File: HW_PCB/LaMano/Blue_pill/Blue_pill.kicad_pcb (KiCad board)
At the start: 2 copper layers, 41.1 x 42.8 mm, 28 parts, among them J1 V_Battery, J2 STLINK, J5 MPU6050, J6 NRF24, SW1 SW_DPST_x2, SW2 SW_DPST_x2, U1 STM32F103C8Tx, U2 AMS1117-3.3, X1 Crystal

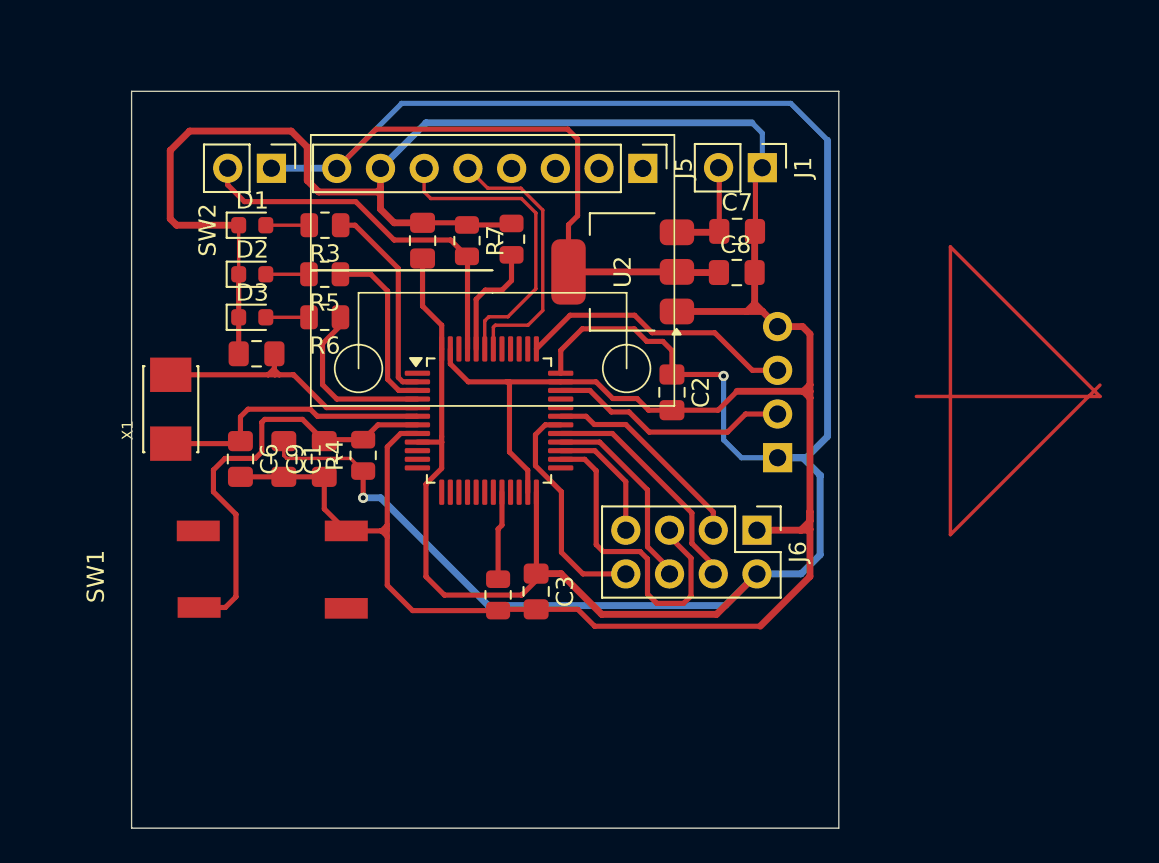
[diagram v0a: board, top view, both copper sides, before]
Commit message: DRC 0 Errors (Board cleareance errors, Fix: Increased Board size) Fixed mismatch size on 2 gnd tracks
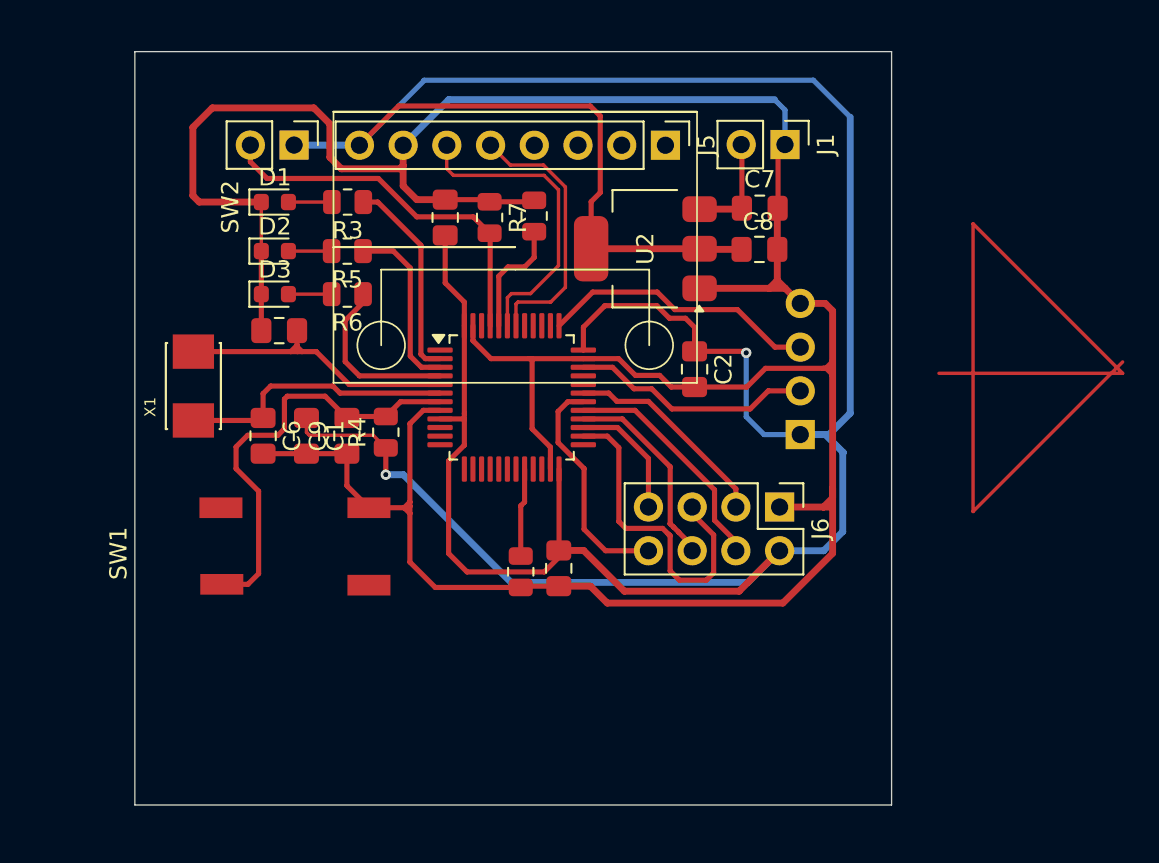
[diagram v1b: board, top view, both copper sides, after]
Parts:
- moved C1 1.88 mm to (48.8, 62.4)
- moved C3 1.88 mm to (63.4, 70.1)
- moved C5 1.88 mm to (47.2, 56.3)
- moved C6 1.88 mm to (46.3, 62.4)
- moved C7 1.88 mm to (75.1, 49.2)
- moved C8 1.88 mm to (75.1, 51.6)
- moved C9 1.88 mm to (51.1, 62.4)
- moved D1 1.88 mm to (47.0, 48.9)
- moved J1 1.88 mm to (76.6, 45.5)
- moved J2 1.88 mm to (77.5, 62.4)
- moved J5 1.88 mm to (69.6, 45.6)
- moved J6 1.88 mm to (76.3, 66.6)
- moved R1 1.88 mm to (61.2, 70.3)
- moved R2 1.88 mm to (62.0, 49.7)
- moved R3 1.88 mm to (51.2, 48.9)
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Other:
- board size 41.1 x 42.8 mm -> 44 x 43.8 mm

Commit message: 6-29 Added Potentiometer Added Voltage divider for Battery Sensor Changed Layer tracks of NRF24
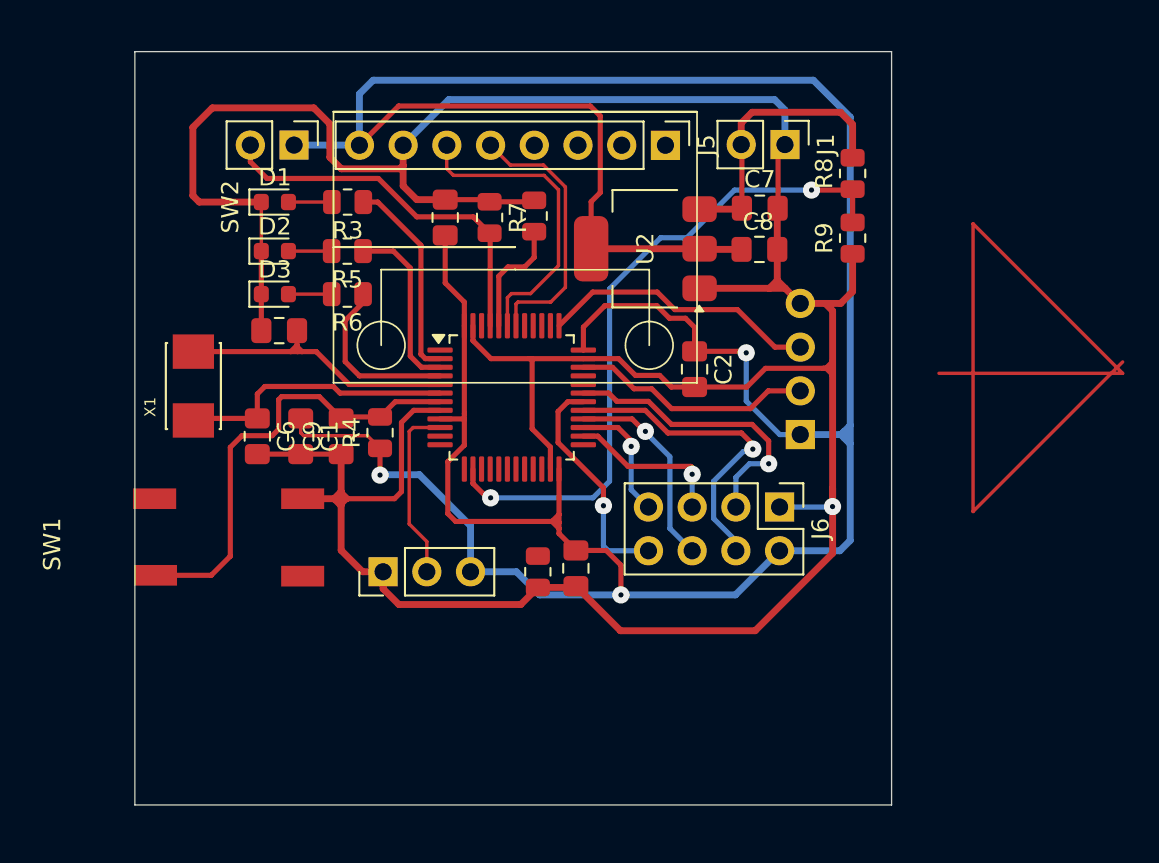
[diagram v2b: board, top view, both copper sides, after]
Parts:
- added J8: PINHD_1x3_Male, Connector_PinHeader_2.54mm:PinHeader_1x03_P2.54mm_Vertical, F.Cu at (53.2, 70.3)
- added R8: PORDEFINIR, Resistor_SMD:R_0805_2012Metric, F.Cu at (80.5, 47.2)
- added R9: PORDEFINIR, Resistor_SMD:R_0805_2012Metric, F.Cu at (80.5, 51.0)
- moved SW1 3.89 mm to (34.5, 68.7)
- moved C3 0.99 mm to (64.4, 70.1)
- moved R1 0.99 mm to (62.2, 70.3)
- moved C6 0.34 mm to (45.9, 62.5)
- moved C9 0.34 mm to (50.8, 62.5)
- moved C1 0.34 mm to (48.5, 62.5)
- moved R4 0.34 mm to (53.1, 62.3)
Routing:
- net ADC2: track 0.00 -> 39.4 mm, vias 0 -> 2
- net GND: track 184.0 -> 197.5 mm, vias 0 -> 1
- net ADC1: track 0.00 -> 10.5 mm
- net VIN: track 6.20 -> 16.4 mm
- net SCK: track 19.3 -> 9.74 mm, vias 0 -> 1
- net VCC: track 201.9 -> 195.6 mm, vias 2 -> 3
- net Net-(U1-PB2): track 5.15 -> 0.00 mm
- net CSN: track 13.6 -> 18.6 mm, vias 0 -> 1
- net CE: track 12.2 -> 17.2 mm, vias 0 -> 1
- net NRST: track 25.4 -> 26.6 mm
- net MOSI: track 11.6 -> 12.3 mm, vias 0 -> 1
- net IRQ: track 14.2 -> 14.1 mm, vias 0 -> 1
- net MISO: track 7.35 -> 7.36 mm, vias 0 -> 1

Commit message: 6-29 DRC Check Connect Resistor on PB2
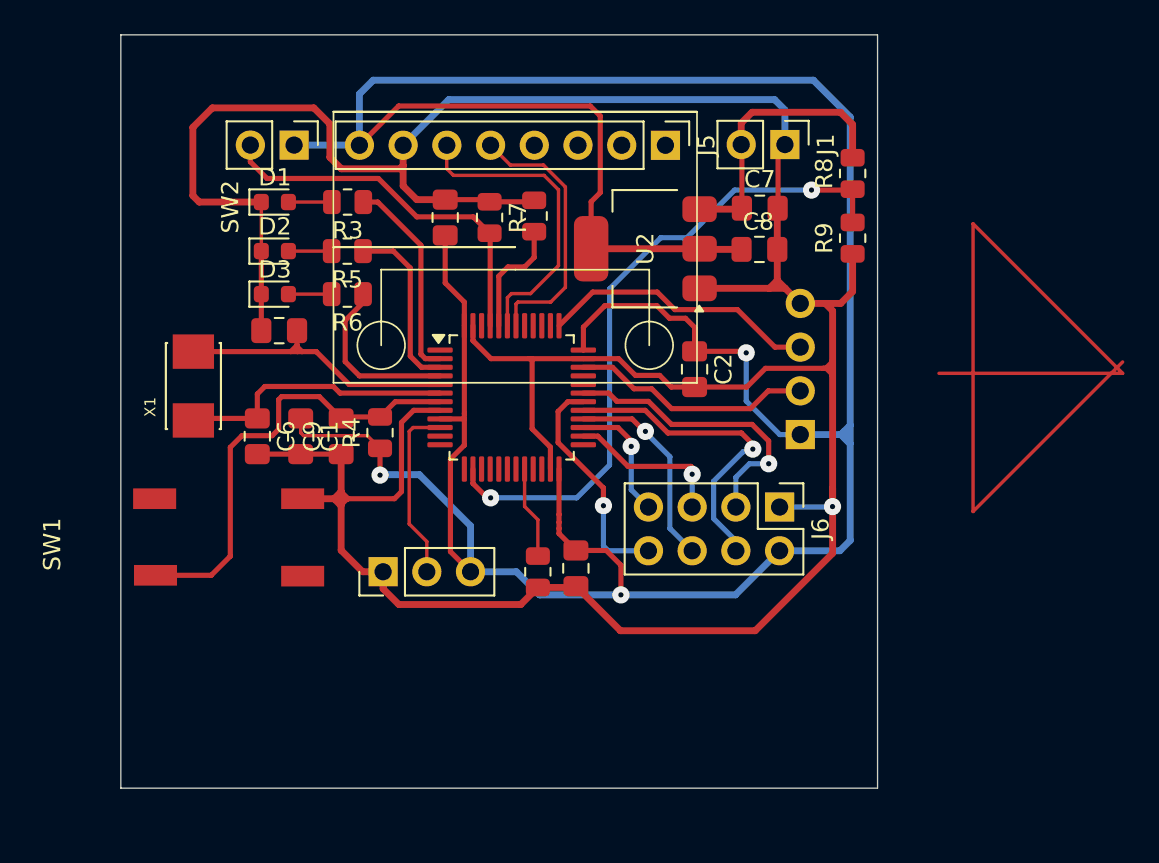
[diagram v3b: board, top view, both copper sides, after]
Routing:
- net Net-(U1-PB2): track 0.00 -> 5.37 mm
- net VCC: track 195.6 -> 191.5 mm
- net ADC2: track 39.4 -> 38.8 mm
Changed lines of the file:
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@@
 		)
 		(property "Value" "STLINK"
-			(at -22.05 26.875 0)
+			(at -22.8655 25.9005 0)
 			(layer "B.Fab")
 			(effects
@@
 	)
 	(gr_rect
-		(start 38.8155 40.1146)
-		(end 82.781542 83.8845)
+		(start 38 39.1401)
+		(end 81.966042 82.91)
 		(stroke
 			(width 0.05)
@@
 	)
 	(segment
-		(start 57.9593 62.9807)
-		(end 56.9976 63.9424)
-		(width 0.3)
-		(layer "F.Cu")
-		(net "VCC")
-	)
-	(segment
 		(start 57.9593 61.1407)
 		(end 57.9593 61.4645)
@@
 	)
 	(segment
-		(start 63.0428 67.4116)
-		(end 63.4085 67.4116)
-		(width 0.3)
-		(layer "F.Cu")
-		(net "VCC")
-	)
-	(segment
-		(start 63.0529 67.4116)
-		(end 63.4593 67.818)
-		(width 0.3)
-		(layer "F.Cu")
-		(net "VCC")
-	)
-	(segment
 		(start 63.4593 64.367)
 		(end 63.4593 67.0052)
@@
 	)
 	(segment
-		(start 57.4548 67.4116)
-		(end 63.0428 67.4116)
+		(start 57.15 69.1661)
+		(end 57.15 63.79)
 		(width 0.3)
 		(layer "F.Cu")
@@
 	)
 	(segment
-		(start 63.0428 67.4116)
-		(end 63.0529 67.4116)
-		(width 0.3)
-		(layer "F.Cu")
-		(net "VCC")
-	)
-	(segment
 		(start 64.8755 56.1245)
 		(end 64.8755 57.4508)
@@
 	)
 	(segment
+		(start 57.15 63.79)
+		(end 57.9593 62.9807)
+		(width 0.3)
+		(layer "F.Cu")
+		(net "VCC")
+	)
+	(segment
 		(start 54.1418 43.2745)
 		(end 65.2755 43.2745)
@@
 	)
 	(segment
+		(start 58.3184 70.3345)
+		(end 57.15 69.1661)
+		(width 0.3)
+		(layer "F.Cu")
+		(net "VCC")
+	)
+	(segment
 		(start 65.1571 51.3986)
 		(end 65.3255 51.567)
@@
 	)
 	(segment
-		(start 57.9593 61.4645)
-		(end 57.9593 62.9807)
+		(start 57.9593 62.9807)
+		(end 57.9593 61.4645)
 		(width 0.3)
 		(layer "F.Cu")
@@
 	)
 	(segment
-		(start 56.9976 63.9424)
-		(end 56.9976 66.9544)
-		(width 0.3)
-		(layer "F.Cu")
-		(net "VCC")
-	)
-	(segment
 		(start 74.248 57.527)
 		(end 74.3355 57.6145)
@@
 	)
 	(segment
-		(start 63.4085 67.4116)
-		(end 63.4593 67.4624)
-		(width 0.3)
-		(layer "F.Cu")
-		(net "VCC")
-	)
-	(segment
 		(start 56.8455 50.7895)
 		(end 56.8455 53.5545)
@@
 	)
 	(segment
-		(start 63.0529 67.4116)
-		(end 63.4593 67.0052)
-		(width 0.3)
-		(layer "F.Cu")
-		(net "VCC")
-	)
-	(segment
-		(start 56.9976 66.9544)
-		(end 57.4548 67.4116)
-		(width 0.3)
-		(layer "F.Cu")
-		(net "VCC")
-	)
-	(segment
 		(start 65.8555 43.8545)
 		(end 65.8555 48.30589)
@@
 	)
 	(segment
-		(start 78.1304 48.1584)
-		(end 73.66 48.1584)
+		(start 70.8914 50.927)
+		(end 69.3674 50.927)
 		(width 0.3)
 		(layer "B.Cu")
@@
 	)
 	(segment
-		(start 66.3956 65.0748)
-		(end 65.4304 66.04)
+		(start 78.1304 48.1584)
+		(end 73.66 48.1584)
 		(width 0.3)
 		(layer "B.Cu")
@@
 	(segment
 		(start 66.3956 53.8988)
-		(end 66.3956 65.0748)
+		(end 66.3956 64.135)
 		(width 0.3)
 		(layer "B.Cu")
@@
 	)
 	(segment
-		(start 70.8914 50.927)
-		(end 70.7644 51.054)
+		(start 64.4906 66.04)
+		(end 66.3956 64.135)
 		(width 0.3)
 		(layer "B.Cu")
@@
 	)
 	(segment
-		(start 73.66 48.1584)
-		(end 70.8914 50.927)
+		(start 70.8914 50.927)
+		(end 70.7644 51.054)
 		(width 0.3)
 		(layer "B.Cu")
@@
 	)
 	(segment
-		(start 65.4304 66.04)
-		(end 59.436 66.04)
+		(start 73.66 48.1584)
+		(end 70.8914 50.927)
 		(width 0.3)
 		(layer "B.Cu")
@@
 	)
 	(segment
-		(start 70.8914 50.927)
-		(end 69.3674 50.927)
+		(start 59.4868 66.04)
+		(end 64.4906 66.04)
 		(width 0.3)
 		(layer "B.Cu")
@@
 	)
 	(segment
+		(start 62.23 67.31)
+		(end 62.23 69.422)
+		(width 0.2)
+		(layer "F.Cu")
+		(net "Net-(U1-PB2)")
+	)
+	(segment
+		(start 61.4593 64.367)
+		(end 61.4593 66.5393)
+		(width 0.2)
+		(layer "F.Cu")
+		(net "Net-(U1-PB2)")
+	)
+	(segment
+		(start 61.4593 66.5393)
+		(end 62.23 67.31)
+		(width 0.2)
+		(layer "F.Cu")
+		(net "Net-(U1-PB2)")
+	)
+	(segment

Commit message: 6-29 Fixed MPU orientation Added Vias
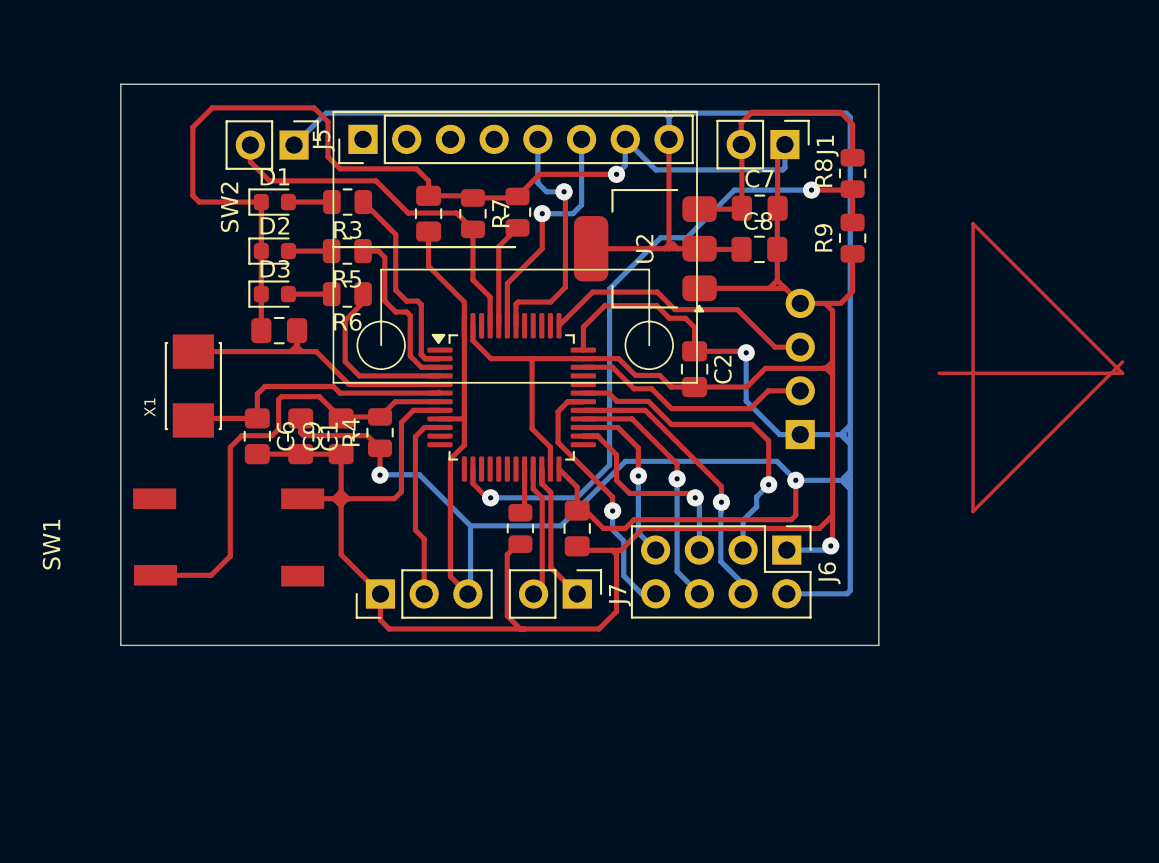
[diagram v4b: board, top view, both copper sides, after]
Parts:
- added J7: UART, Connector_PinHeader_2.54mm:PinHeader_1x02_P2.54mm_Vertical, F.Cu at (64.5, 71.6)
- moved J5 17.6 mm to (52.1, 45.2), turned to 90 degrees
- moved R1 2.71 mm to (61.2, 67.8)
- moved J6 2.54 mm to (76.7, 69.1)
- moved C3 2.32 mm to (64.5, 67.8)
- moved J8 1.30 mm to (53.1, 71.6)
- moved R2 0.99 mm to (61.0, 49.4)
- moved C4 0.99 mm to (55.9, 49.5)
- moved R7 0.99 mm to (58.5, 49.5)
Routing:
- net RX: track 0.00 -> 9.00 mm
- net TX: track 0.00 -> 7.69 mm
- net SCL: track 18.1 -> 13.7 mm, vias 0 -> 1
- net SCK: track 9.74 -> 13.2 mm
- net MISO: track 7.36 -> 10.3 mm
- net Net-(U1-PB2): track 5.37 -> 2.64 mm
- net MOSI: track 12.3 -> 14.9 mm
- net VCC: track 191.5 -> 193.3 mm
- net IRQ: track 14.1 -> 15.9 mm
- net CE: track 17.2 -> 18.9 mm
- net CSN: track 18.6 -> 17.1 mm
- net GND: track 197.5 -> 198.8 mm, vias 1 -> 2
- net RED: track 11.9 -> 13.0 mm
- net SDA: track 15.7 -> 14.6 mm, vias 0 -> 1
- net Net-(U1-BOOT0): track 6.88 -> 6.14 mm
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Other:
- board size 44 x 43.8 mm -> 44 x 32.6 mm
